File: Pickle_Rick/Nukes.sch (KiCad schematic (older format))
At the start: 21 parts, among them J6 Screw_Terminal_01x02, J7 Screw_Terminal_01x02, J8 Screw_Terminal_01x02, Q4 PMV20ENR, Q5 PMV20ENR, U10 LTV-817S, U9 LTV-817S

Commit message: updated optocoupler, usb kinda weird atm ¯\_(ツ)_/¯
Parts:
- removed U10, U9: LTV-817S, Package_DIP:SMDIP-4_W9.53mm, symbol Isolator:LTV-817S
- added U? (x2): LTV-354T, Package_SO:SO-4_4.4x3.6mm_P2.54mm, symbol Isolator:LTV-354T
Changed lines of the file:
@@
 Wire Wire Line
 	8600 4150 8600 4200
-$Comp
-L Isolator:LTV-817S U?
-U 1 1 5DE04B23
-P 9450 4700
-AR Path="/5DDE6CFA/5DE04B23" Ref="U?"  Part="1"
-AR Path="/5DDE1103/5DE04B23" Ref="U10"  Part="1"
-F 0 "U10" H 9450 5025 50  0000 C CNN
-F 1 "LTV-817S" H 9450 4934 50  0000 C CNN
-F 2 "Package_DIP:SMDIP-4_W9.53mm" H 9450 4400 50  0001 C CNN
-F 3 "http://www.us.liteon.com/downloads/LTV-817-827-847.PDF" H 9100 5000 50  0001 C CNN
-	1    9450 4700
-	-1   0    0    -1
-$EndComp
 Wire Wire Line
 	9750 4150 9750 4600
@@
 Wire Wire Line
 	4350 4300 4350 4350
-$Comp
-L Isolator:LTV-817S U?
-U 1 1 5DE32360
-P 5200 4850
-AR Path="/5DDE6CFA/5DE32360" Ref="U?"  Part="1"
-AR Path="/5DDE1103/5DE32360" Ref="U9"  Part="1"
-F 0 "U9" H 5200 5175 50  0000 C CNN
-F 1 "LTV-817S" H 5200 5084 50  0000 C CNN
-F 2 "Package_DIP:SMDIP-4_W9.53mm" H 5200 4550 50  0001 C CNN
-F 3 "http://www.us.liteon.com/downloads/LTV-817-827-847.PDF" H 4850 5150 50  0001 C CNN
-	1    5200 4850
-	-1   0    0    -1
-$EndComp
 Wire Wire Line
 	5500 4300 5500 4750
@@
 Wire Wire Line
 	5450 2600 6350 2600
+$Comp
+L Isolator:LTV-354T U?
+U 1 1 603DC15B
+P 5200 4850
+F 0 "U?" H 5200 5175 50  0000 C CNN
+F 1 "LTV-354T" H 5200 5084 50  0000 C CNN
+F 2 "Package_SO:SO-4_4.4x3.6mm_P2.54mm" H 5000 4650 50  0001 L CIN
+F 3 "http://optoelectronics.liteon.com/upload/download/DS70-2001-004/S_110_LTV-354T%2020140520.pdf" H 5225 4850 50  0001 L CNN
+	1    5200 4850
+	1    0    0    -1
+$EndComp
+$Comp
+L Isolator:LTV-354T U?
+U 1 1 603EA371
+P 9450 4700
+F 0 "U?" H 9450 5025 50  0000 C CNN
+F 1 "LTV-354T" H 9450 4934 50  0000 C CNN
+F 2 "Package_SO:SO-4_4.4x3.6mm_P2.54mm" H 9250 4500 50  0001 L CIN
+F 3 "http://optoelectronics.liteon.com/upload/download/DS70-2001-004/S_110_LTV-354T%2020140520.pdf" H 9475 4700 50  0001 L CNN
+	1    9450 4700
+	1    0    0    -1
+$EndComp
 $EndSCHEMATC

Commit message: 50/50 that the usb will work
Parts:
- gave numbers to parts that had none: 2
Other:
- moved on the sheet: D14, D15, D16, J7, J8, Q5, R32, R33, R34, R35, U10

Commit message: fixed led circuit/made sure cc pins are independent
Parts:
- J6, J7, J8: footprint iclr-hw:PHOENIX_1757242 -> iclr:PHOENIX_1757242
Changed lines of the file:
@@
 F 0 "J7" H 4218 2425 50  0000 C CNN
 F 1 "Screw_Terminal_01x02" H 4218 2516 50  0000 C CNN
-F 2 "iclr-hw:PHOENIX_1757242" H 4300 2750 50  0001 C CNN
+F 2 "iclr:PHOENIX_1757242" H 4300 2750 50  0001 C CNN
 F 3 "~" H 4300 2750 50  0001 C CNN
 	1    4300 2750
@@
 F 0 "J8" V 7564 3812 50  0000 R CNN
 F 1 "Screw_Terminal_01x02" V 7473 3812 50  0000 R CNN
-F 2 "iclr-hw:PHOENIX_1757242" H 7600 4000 50  0001 C CNN
+F 2 "iclr:PHOENIX_1757242" H 7600 4000 50  0001 C CNN
 F 3 "~" H 7600 4000 50  0001 C CNN
 	1    7600 4000
@@
 F 0 "J6" V 4164 3862 50  0000 R CNN
 F 1 "Screw_Terminal_01x02" V 4073 3862 50  0000 R CNN
-F 2 "iclr-hw:PHOENIX_1757242" H 4200 4050 50  0001 C CNN
+F 2 "iclr:PHOENIX_1757242" H 4200 4050 50  0001 C CNN
 F 3 "~" H 4200 4050 50  0001 C CNN
 	1    4200 4050

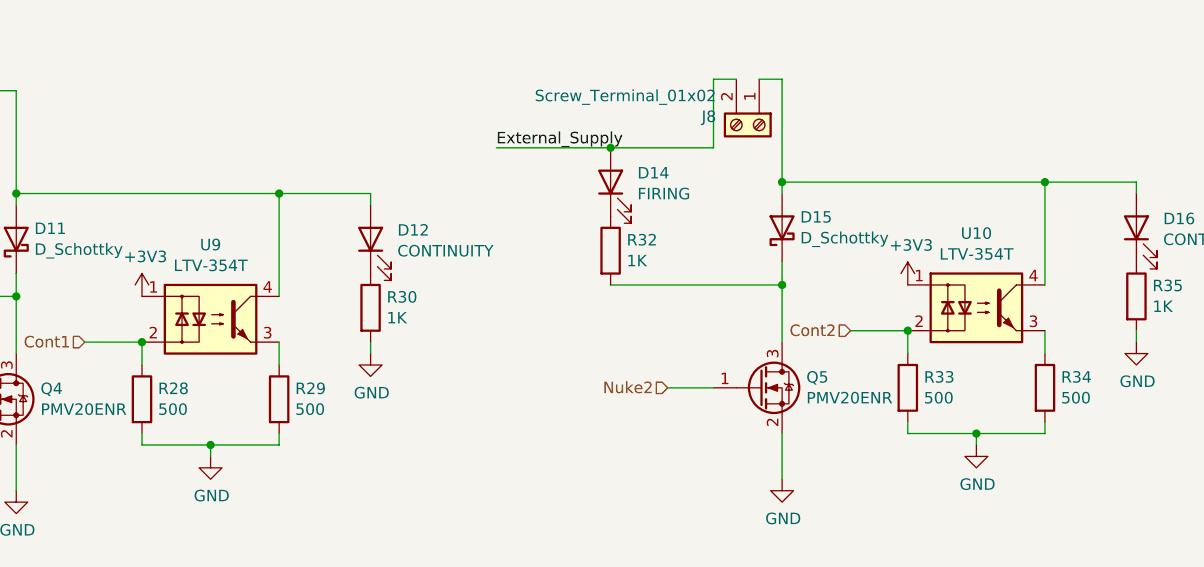
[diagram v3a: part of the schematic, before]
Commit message: changed to single 2 channel optocoupler
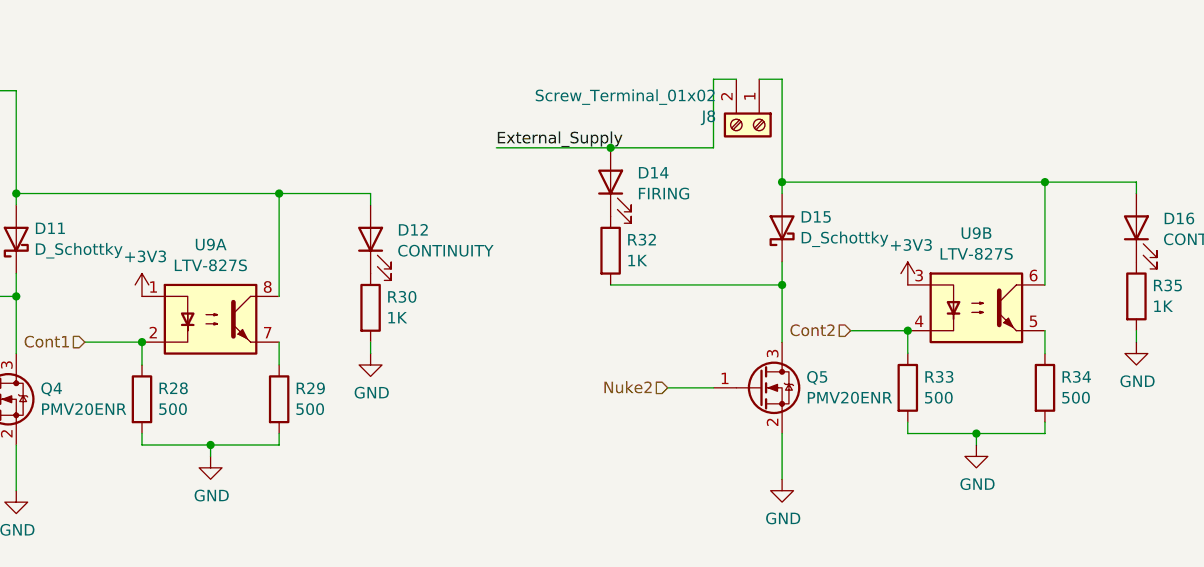
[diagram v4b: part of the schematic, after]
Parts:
- removed U10, U9: LTV-354T, Package_SO:SO-4_4.4x3.6mm_P2.54mm, symbol Isolator:LTV-354T
- added U9: LTV-827S, Package_DIP:SMDIP-8_W9.53mm, symbol Isolator:LTV-827S
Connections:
- net +3V3: now also U9.1, U9.3
- net Cont1: now also U9.2
- net Cont2: now also U9.4
- net at D15.2 (A), D16.2 (A), J8.1 (Pin_1): now also U9.6
- net at R34.1: now also U9.5
- net at D11.2 (A), D12.2 (A), J6.1 (Pin_1): now also U9.8
- net at R29.1: now also U9.7
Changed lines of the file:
@@
 	4500 2750 5400 2750
 $Comp
-L Isolator:LTV-354T U9
-U 1 1 603DC15B
+L Isolator:LTV-827S U9
+U 1 1 6045E90E
 P 5200 4850
 F 0 "U9" H 5200 5175 50  0000 C CNN
-F 1 "LTV-354T" H 5200 5084 50  0000 C CNN
-F 2 "Package_SO:SO-4_4.4x3.6mm_P2.54mm" H 5000 4650 50  0001 L CIN
-F 3 "http://optoelectronics.liteon.com/upload/download/DS70-2001-004/S_110_LTV-354T%2020140520.pdf" H 5225 4850 50  0001 L CNN
+F 1 "LTV-827S" H 5200 5084 50  0000 C CNN
+F 2 "Package_DIP:SMDIP-8_W9.53mm" H 5200 4550 50  0001 C CNN
+F 3 "http://www.us.liteon.com/downloads/LTV-817-827-847.PDF" H 4400 5400 50  0001 C CNN
 	1    5200 4850
 	1    0    0    -1
 $EndComp
 $Comp
-L Isolator:LTV-354T U10
-U 1 1 603EA371
+L Isolator:LTV-827S U9
+U 2 1 604634BA
 P 8550 4800
-F 0 "U10" H 8550 5125 50  0000 C CNN
-F 1 "LTV-354T" H 8550 5034 50  0000 C CNN
-F 2 "Package_SO:SO-4_4.4x3.6mm_P2.54mm" H 8350 4600 50  0001 L CIN
-F 3 "http://optoelectronics.liteon.com/upload/download/DS70-2001-004/S_110_LTV-354T%2020140520.pdf" H 8575 4800 50  0001 L CNN
-	1    8550 4800
+F 0 "U9" H 8550 5125 50  0000 C CNN
+F 1 "LTV-827S" H 8550 5034 50  0000 C CNN
+F 2 "Package_DIP:SMDIP-8_W9.53mm" H 8550 4500 50  0001 C CNN
+F 3 "http://www.us.liteon.com/downloads/LTV-817-827-847.PDF" H 7750 5350 50  0001 C CNN
+	2    8550 4800
 	1    0    0    -1
 $EndComp

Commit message: todo: change everything ᕙ(⇀‸↼‶)ᕗ
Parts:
- J6, J7, J8: footprint iclr:PHOENIX_1757242 -> TerminalBlock_Phoenix:TerminalBlock_Phoenix_PT-1,5-2-5.0-H_1x02_P5.00mm_Horizontal
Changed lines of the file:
@@
 F 0 "J7" H 4218 2425 50  0000 C CNN
 F 1 "Screw_Terminal_01x02" H 4218 2516 50  0000 C CNN
-F 2 "iclr:PHOENIX_1757242" H 4300 2750 50  0001 C CNN
+F 2 "TerminalBlock_Phoenix:TerminalBlock_Phoenix_PT-1,5-2-5.0-H_1x02_P5.00mm_Horizontal" H 4300 2750 50  0001 C CNN
 F 3 "~" H 4300 2750 50  0001 C CNN
 	1    4300 2750
@@
 F 0 "J8" V 7564 3812 50  0000 R CNN
 F 1 "Screw_Terminal_01x02" V 7473 3812 50  0000 R CNN
-F 2 "iclr:PHOENIX_1757242" H 7600 4000 50  0001 C CNN
+F 2 "TerminalBlock_Phoenix:TerminalBlock_Phoenix_PT-1,5-2-5.0-H_1x02_P5.00mm_Horizontal" H 7600 4000 50  0001 C CNN
 F 3 "~" H 7600 4000 50  0001 C CNN
 	1    7600 4000
@@
 F 0 "J6" V 4164 3862 50  0000 R CNN
 F 1 "Screw_Terminal_01x02" V 4073 3862 50  0000 R CNN
-F 2 "iclr:PHOENIX_1757242" H 4200 4050 50  0001 C CNN
+F 2 "TerminalBlock_Phoenix:TerminalBlock_Phoenix_PT-1,5-2-5.0-H_1x02_P5.00mm_Horizontal" H 4200 4050 50  0001 C CNN
 F 3 "~" H 4200 4050 50  0001 C CNN
 	1    4200 4050
